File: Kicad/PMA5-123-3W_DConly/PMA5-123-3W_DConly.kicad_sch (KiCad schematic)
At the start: 42 parts, among them J1 8V-DC, J2 UPDI, J3 RF_unit, Q1 FMG1, Q2 BC850, SW1 SW_Push, U1 L78L05_SOT89, U2 R05C1TF05S-R, U3 MIC29302, U5 INA168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

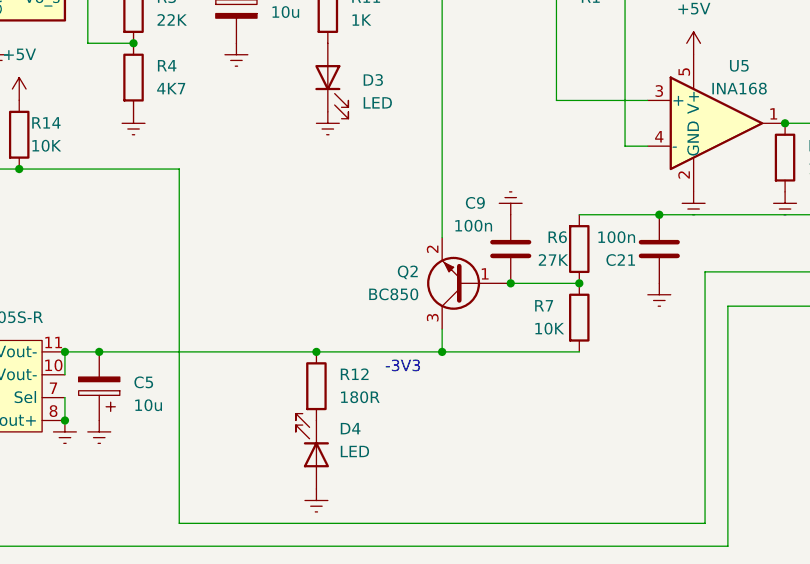
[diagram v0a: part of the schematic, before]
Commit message: Used right symbol in schematic
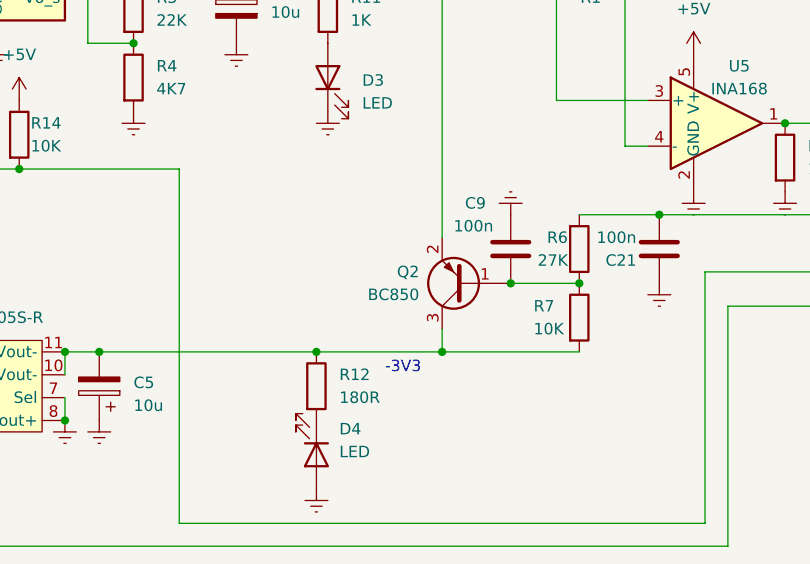
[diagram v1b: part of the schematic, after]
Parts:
- removed Q2: BC850, Package_TO_SOT_SMD:SOT-23, symbol Transistor_BJT:BC850
- added Q2: BC850, Package_TO_SOT_SMD:SOT-23, symbol Device:Q_PNP_BEC
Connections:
- net at C9.2, R6.1, R7.1: now also Q2.1 (B)
- net at C5.2, R12.1, R7.2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: now also Q2.3 (C)
- net at J3.3 (Pin_3): now also Q2.2 (E)
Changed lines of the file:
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@@
     (pin "9")
   )
-  (symbol (lib_id "Transistor_BJT:BC850") (at 144.78 158.75 180) (unit 1)
-    (in_bom yes) (on_board yes)
-    (property "Reference" "Q2" (id 0) (at 139.7 157.48 0)
-      (effects (font (size 1.27 1.27)) (justify left))
-    )
-    (property "Value" "BC850" (id 1) (at 139.7 160.02 0)
-      (effects (font (size 1.27 1.27)) (justify left))
-    )
-    (property "Footprint" "Package_TO_SOT_SMD:SOT-23" (id 2) (at 139.7 156.845 0)
-      (effects (font (size 1.27 1.27) italic) (justify left) hide)
-    )
-    (property "Datasheet" "http://www.infineon.com/dgdl/Infineon-BC847SERIES_BC848SERIES_BC849SERIES_BC850SERIES-DS-v01_01-en.pdf?fileId=db3a304314dca389011541d4630a1657" (id 3) (at 144.78 158.75 0)
-      (effects (font (size 1.27 1.27)) (justify left) hide)
+  (symbol (lib_id "power:GNDREF") (at 82.55 151.13 0) (unit 1)
+    (in_bom yes) (on_board yes) (fields_autoplaced)
+    (property "Reference" "#PWR0101" (id 0) (at 82.55 157.48 0)
+      (effects (font (size 1.27 1.27)) hide)
+    )
+    (property "Value" "GNDREF" (id 1) (at 82.55 156.21 0)
+      (effects (font (size 1.27 1.27)) hide)
+    )
+    (property "Footprint" "" (id 2) (at 82.55 151.13 0)
+      (effects (font (size 1.27 1.27)) hide)
+    )
+    (property "Datasheet" "" (id 3) (at 82.55 151.13 0)
+      (effects (font (size 1.27 1.27)) hide)
+    )
+    (pin "1")
+  )
+  (symbol (lib_id "Device:Q_PNP_BEC") (at 144.78 158.75 180) (unit 1)
+    (in_bom yes) (on_board yes) (fields_autoplaced)
+    (property "Reference" "Q2" (id 0) (at 139.7 157.4799 0)
+      (effects (font (size 1.27 1.27)) (justify left))
+    )
+    (property "Value" "BC850" (id 1) (at 139.7 160.0199 0)
+      (effects (font (size 1.27 1.27)) (justify left))
+    )
+    (property "Footprint" "Package_TO_SOT_SMD:SOT-23" (id 2) (at 139.7 161.29 0)
+      (effects (font (size 1.27 1.27)) hide)
+    )
+    (property "Datasheet" "~" (id 3) (at 144.78 158.75 0)
+      (effects (font (size 1.27 1.27)) hide)
     )
     (pin "1")
     (pin "2")
     (pin "3")
-  )
-  (symbol (lib_id "power:GNDREF") (at 82.55 151.13 0) (unit 1)
-    (in_bom yes) (on_board yes) (fields_autoplaced)
-    (property "Reference" "#PWR0101" (id 0) (at 82.55 157.48 0)
-      (effects (font (size 1.27 1.27)) hide)
-    )
-    (property "Value" "GNDREF" (id 1) (at 82.55 156.21 0)
-      (effects (font (size 1.27 1.27)) hide)
-    )
-    (property "Footprint" "" (id 2) (at 82.55 151.13 0)
-      (effects (font (size 1.27 1.27)) hide)
-    )
-    (property "Datasheet" "" (id 3) (at 82.55 151.13 0)
-      (effects (font (size 1.27 1.27)) hide)
-    )
-    (pin "1")
   )
   (symbol (lib_id "power:+5V") (at 73.66 166.37 0) (unit 1)
@@
   (symbol (lib_id "power:GNDREF") (at 45.72 173.99 0) (unit 1)
     (in_bom yes) (on_board yes) (fields_autoplaced)
-    (property "Reference" "#PWR?" (id 0) (at 45.72 180.34 0)
+    (property "Reference" "#PWR0105" (id 0) (at 45.72 180.34 0)
       (effects (font (size 1.27 1.27)) hide)
     )
@@
     )
     (path "/90094669-9d19-4566-8d95-7602e69180af"
-      (reference "#PWR?") (unit 1) (value "GNDREF") (footprint "")
+      (reference "#PWR0105") (unit 1) (value "GNDREF") (footprint "")
     )
     (path "/6c3b6d11-7d0c-4c45-b548-b172f039b611"
@@
       (reference "Q1") (unit 2) (value "FMG1") (footprint "MyFootprints:SOT-25_HandSoldering")
     )
-    (path "/2bb5522b-6a9b-40de-9b11-da088340d317"
+    (path "/2ecc980d-3d4b-4935-8a32-68259f7a5478"
       (reference "Q2") (unit 1) (value "BC850") (footprint "Package_TO_SOT_SMD:SOT-23")
     )
